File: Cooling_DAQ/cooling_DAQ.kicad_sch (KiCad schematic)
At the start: 57 parts, among them J1 USB_C_Receptacle_USB2.0_16P, J10 PUMP_PWR, J11 FAN_PWR, J12 FAN_PWM, J14 PWR, J2 PROG, J3 Temp_1, J4 Temp_2, J5 CAN, J5 PT, J6 Flow, J8 PUMP_PWM, Q1 2N7002, Q2 2N7002, SW1 SW_SPST, U1 STM32F103C8Tx, U2 AP2204K-ADJ, U3 AP2204K-ADJ, U6 SN65HVD256D, Y1 8M, Y2 32.768k

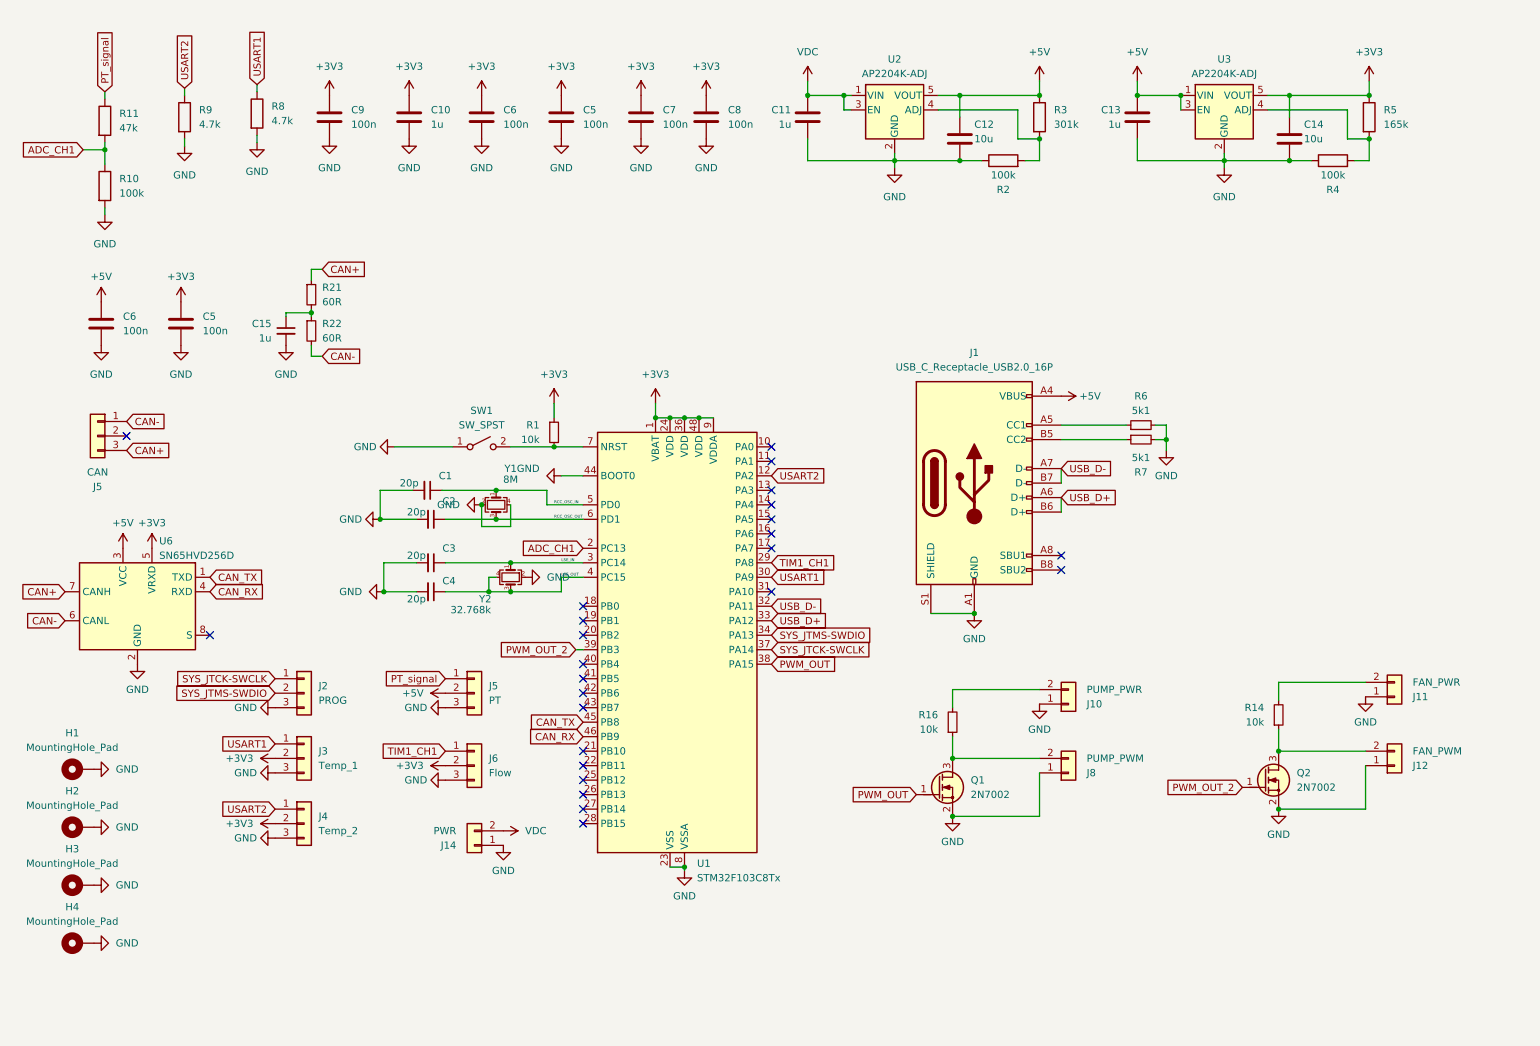
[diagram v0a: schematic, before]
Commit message: update cooling DAQ
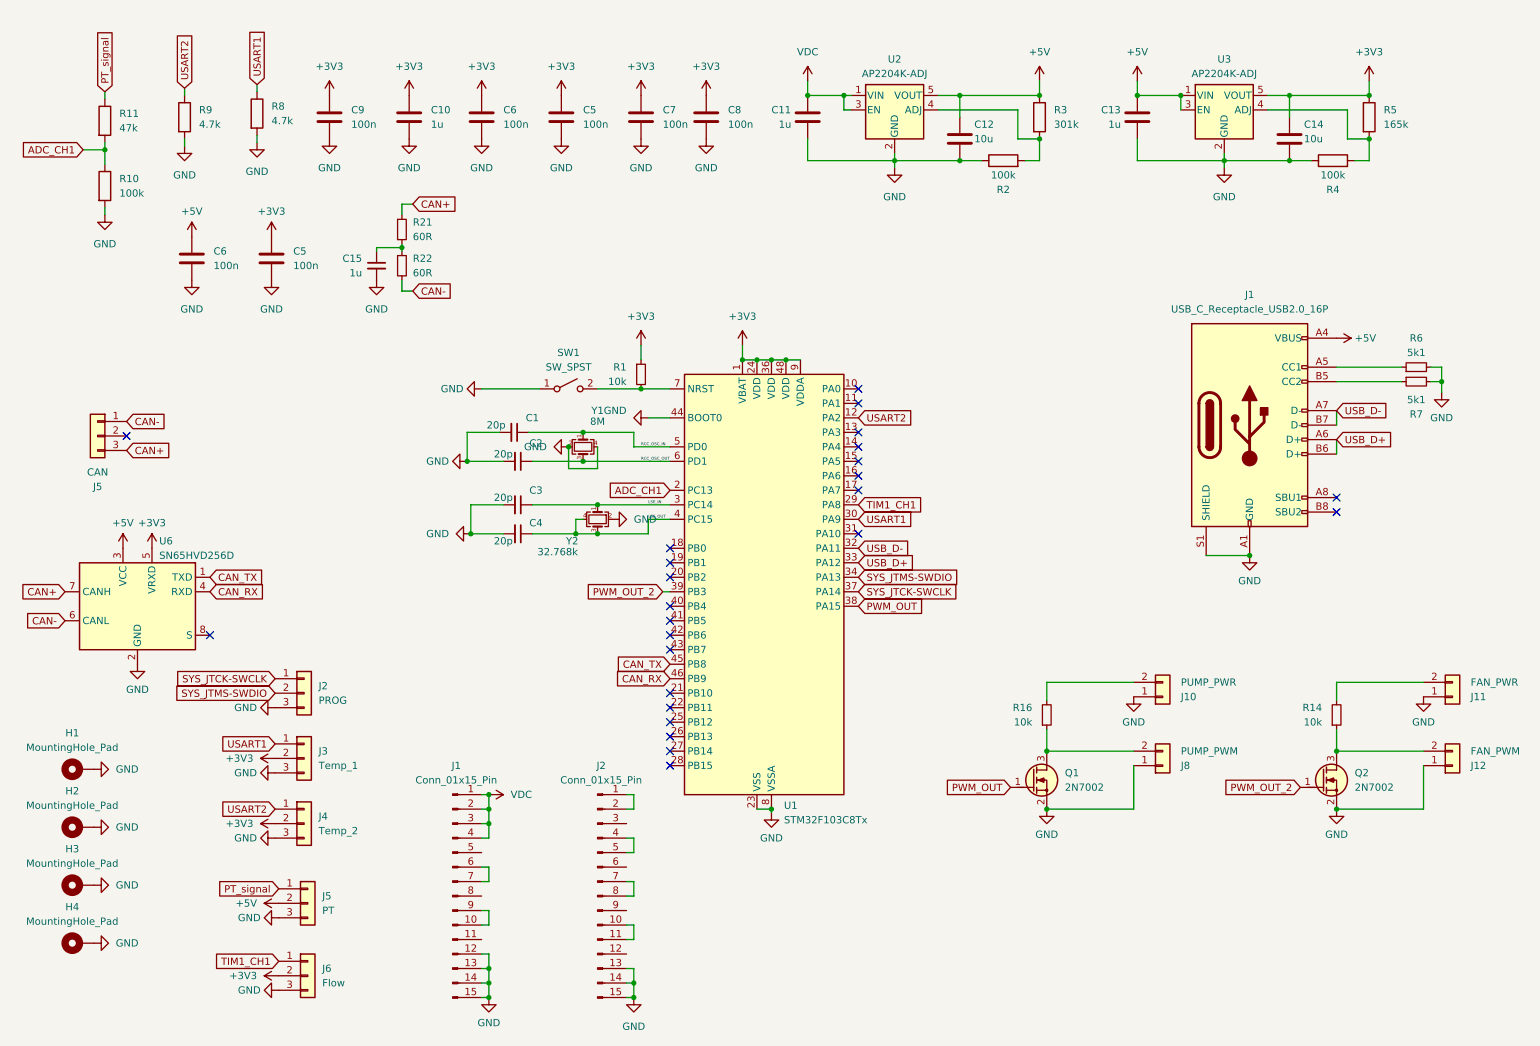
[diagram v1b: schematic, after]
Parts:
- removed J14: PWR, Connector_JST:JST_XH_B2B-XH-A_1x02_P2.50mm_Vertical, symbol Connector_Generic:Conn_01x02
- added J1, J2: Conn_01x15_Pin, Connector_PinHeader_2.54mm:PinHeader_1x15_P2.54mm_Vertical, symbol Connector:Conn_01x15_Pin
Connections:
- net GND: now also J1.12 (Pin_12), J1.13 (Pin_13), J1.14 (Pin_14), J1.15 (Pin_15), J2.13 (Pin_13), J2.14 (Pin_14), J2.15 (Pin_15)
- net VDC: now also J1.1 (Pin_1), J1.2 (Pin_2), J1.3 (Pin_3), J1.4 (Pin_4)
- new net: J2.1 (Pin_1), J2.2 (Pin_2)
- new net: J2.10 (Pin_10), J2.11 (Pin_11)
- new net: J2.4 (Pin_4), J2.5 (Pin_5)
- new net: J2.7 (Pin_7), J2.8 (Pin_8)
- new net: J1.10 (Pin_10), J1.9 (Pin_9)
- new net: J1.6 (Pin_6), J1.7 (Pin_7)
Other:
- moved on the sheet: C1, C15, C2, C3, C4, C5, C6, J1, J10, J11, J12, J5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

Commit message: finish DAQ ver.1
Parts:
- removed J1, J2: Conn_01x15_Pin, Connector_PinHeader_2.54mm:PinHeader_1x15_P2.54mm_Vertical, symbol Connector:Conn_01x15_Pin
- removed J10: PUMP_PWR, Connector_JST:JST_XH_B2B-XH-A_1x02_P2.50mm_Vertical, symbol Connector_Generic:Conn_01x02
- removed J11: FAN_PWR, Connector_JST:JST_XH_B2B-XH-A_1x02_P2.50mm_Vertical, symbol Connector_Generic:Conn_01x02
- removed J12: FAN_PWM, Connector_JST:JST_XH_B2B-XH-A_1x02_P2.50mm_Vertical, symbol Connector_Generic:Conn_01x02
- removed J2: PROG, Connector_PinHeader_2.54mm:PinHeader_1x03_P2.54mm_Vertical, symbol Connector_Generic:Conn_01x03
- removed J3: Temp_1, Connector_JST:JST_XH_B3B-XH-A_1x03_P2.50mm_Vertical, symbol Connector_Generic:Conn_01x03
- removed J4: Temp_2, Connector_JST:JST_XH_B3B-XH-A_1x03_P2.50mm_Vertical, symbol Connector_Generic:Conn_01x03
- removed J5: PT, Connector_JST:JST_XH_B3B-XH-A_1x03_P2.50mm_Vertical, symbol Connector_Generic:Conn_01x03
- removed J5: CAN, Connector_JST:JST_XH_B3B-XH-A_1x03_P2.50mm_Vertical, symbol Connector_Generic:Conn_01x03
- removed J6: Flow, Connector_JST:JST_XH_B3B-XH-A_1x03_P2.50mm_Vertical, symbol Connector_Generic:Conn_01x03
- removed J8: PUMP_PWM, Connector_JST:JST_XH_B2B-XH-A_1x02_P2.50mm_Vertical, symbol Connector_Generic:Conn_01x02
- added J1: Conn_02x10_Odd_Even, Connector_PinHeader_2.54mm:PinHeader_2x10_P2.54mm_Vertical, symbol Connector_Generic:Conn_02x10_Odd_Even
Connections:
- net CAN+: now also J1.20 (Pin_20)
- net CAN-: now also J1.18 (Pin_18)
- net GND: now also J1.15 (Pin_15), J1.17 (Pin_17), J1.19 (Pin_19)
- net PT_signal: now also J1.8 (Pin_8)
- net SYS_JTCK-SWCLK: now also J1.10 (Pin_10)
- net SYS_JTMS-SWDIO: now also J1.12 (Pin_12)
- net TIM1_CH1: now also J1.13 (Pin_13)
- net USART1: now also J1.16 (Pin_16)
- net USART2: now also J1.2 (Pin_2)
- net VDC: now also J1.1 (Pin_1), J1.3 (Pin_3), J1.5 (Pin_5)
- net PUMP_PWR: now reaches R16.2
- net PUMP_PWR: now also J1.7 (Pin_7)
- net PUMP_PWM: now reaches Q1.3 (D), R16.1
- net PUMP_PWM: now also J1.6 (Pin_6)
- net FAN_PWM: now reaches Q2.3 (D), R14.1
- net FAN_PWM: now also J1.4 (Pin_4)
- net FAN_PWR: now reaches R14.2
- net FAN_PWR: now also J1.9 (Pin_9)
- no-connect marks 25 -> 24
